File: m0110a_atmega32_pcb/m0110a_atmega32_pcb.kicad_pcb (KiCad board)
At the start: 2 copper layers, 17.8 x 53.3 mm, 9 parts, among them J1 Conn_01x40_Pin, J2 ISP, J3 Serial, U2 ATmega32A-M, Y1 8 MHz

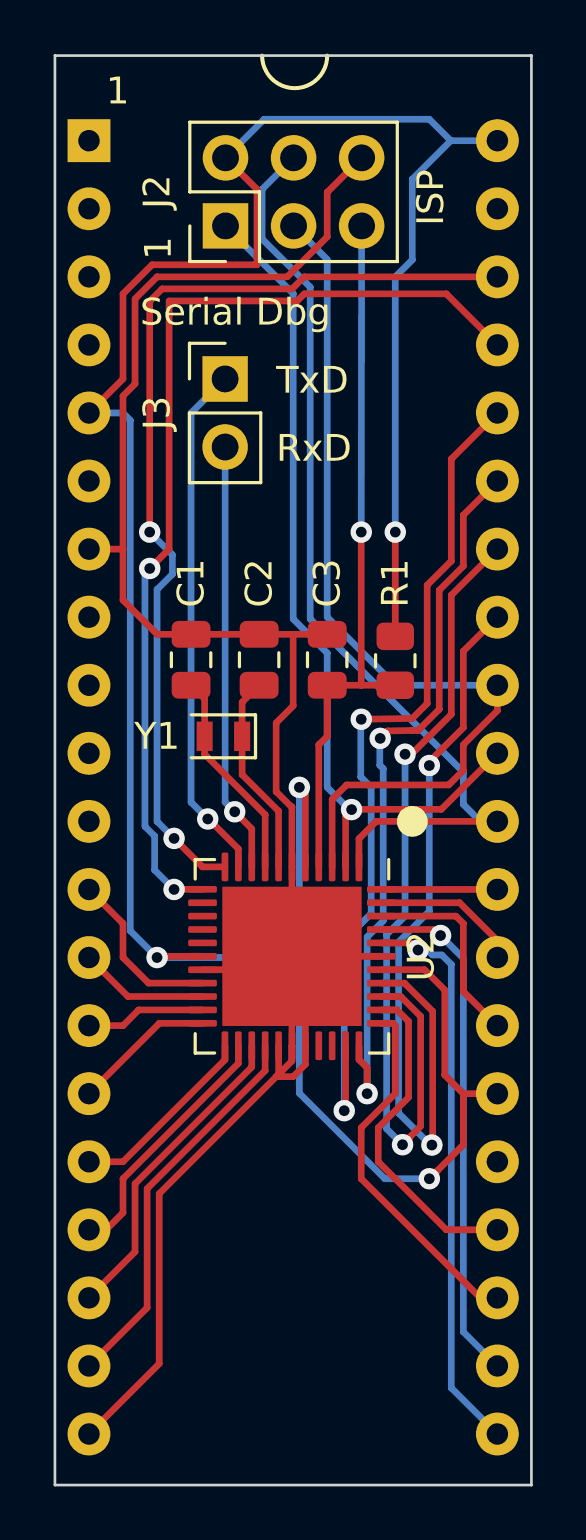
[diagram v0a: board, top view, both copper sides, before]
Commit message: Updated PCB to use more readily available parts
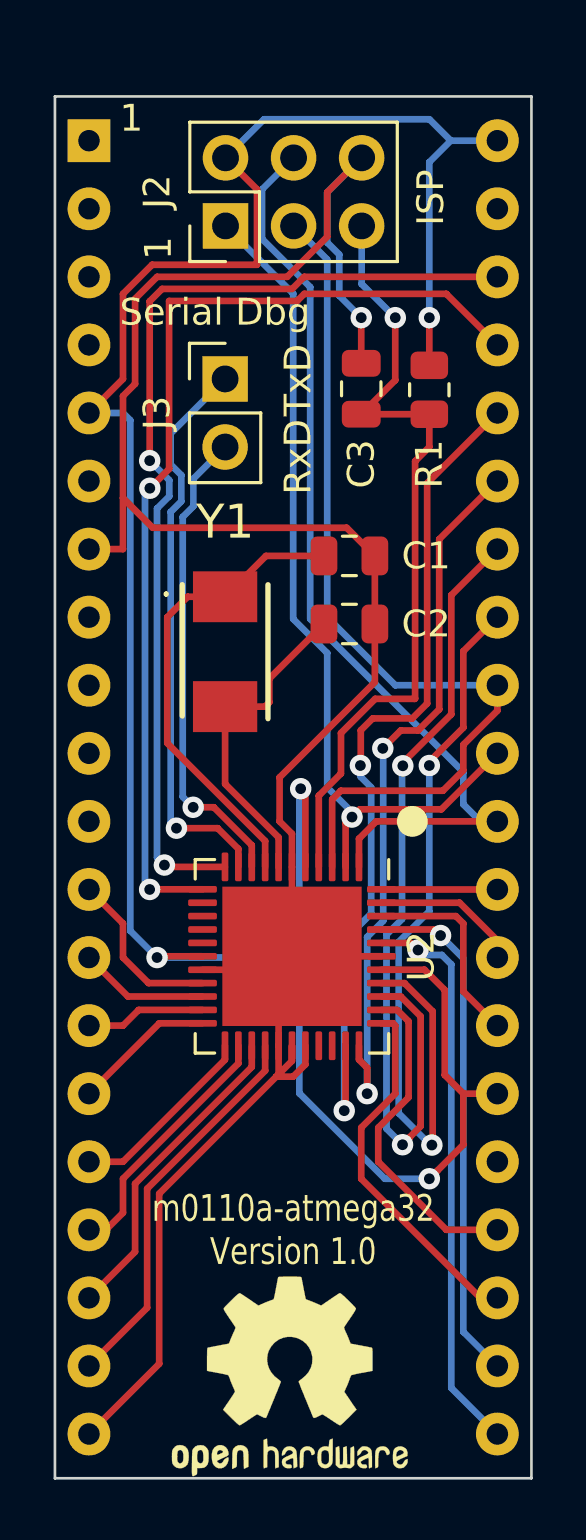
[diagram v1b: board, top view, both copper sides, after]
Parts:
- added REF**: OSHW-Logo2_9.8x8mm_SilkScreen, Symbol:OSHW-Logo2_9.8x8mm_SilkScreen, F.Cu at (151.0, 113.4)
- J1: footprint m0110a:Conn_2.54_W15.24mm -> m0110a:Header_2.54_W15.24mm
- Y1: value 8 MHz -> ABM3-8.000MHZ-D2Y-T; footprint Crystal:Crystal_SMD_2012-2Pin_2.0x1.2mm -> m0110a:ABM3
- moved C3 10.2 mm to (153.7, 76.6)
- moved R1 10.2 mm to (156.2, 76.6)
- moved C1 7.07 mm to (153.2, 82.8), turned to 180 degrees
- moved C2 3.62 mm to (153.2, 85.3), turned to 180 degrees
- moved Y1 3.16 mm to (148.6, 86.4), turned to -90 degrees
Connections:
- Y1 pad 1: Net-(U2-XTAL2) -> Net-(U2-XTAL1)
- Y1 pad 2: Net-(U2-XTAL1) -> Net-(U2-XTAL2)
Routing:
- net +5V: track 108.9 -> 98.1 mm
- net Net-(U2-XTAL1): track 7.92 -> 17.6 mm
- net GNDREF: track 81.4 -> 91.1 mm, vias 0 -> 1
- net Net-(U2-XTAL2): track 7.60 -> 12.3 mm
- net /RESET: track 26.6 -> 30.1 mm
- net /TXD: track 19.5 -> 21.3 mm
- net /RXD: track 16.1 -> 17.8 mm
- net /KB_DATA: track 36.6 -> 37.3 mm
- net /KB_CLK: track 37.0 -> 37.5 mm
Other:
- board size 17.8 x 53.3 mm -> 17.8 x 51.6 mm
- board text added: "github.com/esheffield/m0110a-atmega32"
- board text added: "m0110a-atmega32 Version 1.0"

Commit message: Switched from external to internal clocking
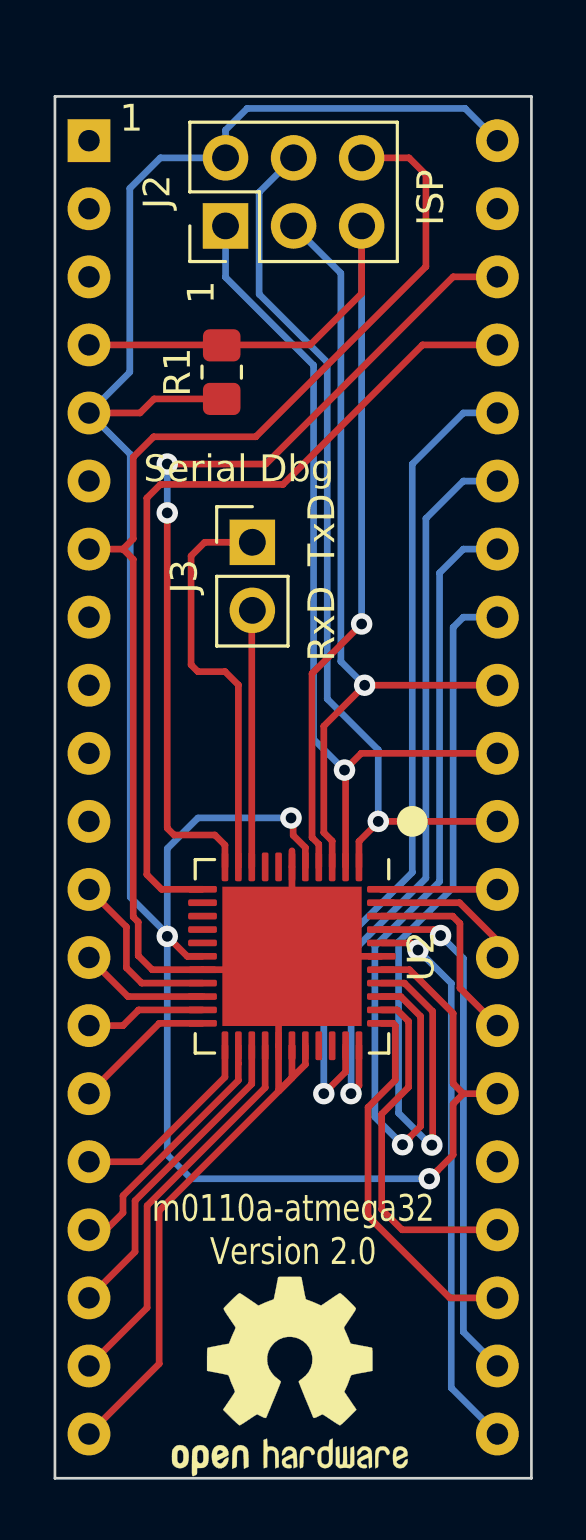
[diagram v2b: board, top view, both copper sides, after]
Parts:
- removed C1, C2: 22p, Capacitor_SMD:C_0805_2012Metric
- removed C3: 1u, Capacitor_SMD:C_0805_2012Metric
- removed Y1: ABM3-8.000MHZ-D2Y-T, m0110a:ABM3
- R1: footprint Resistor_SMD:R_0805_2012Metric -> Resistor_SMD:R_0805_2012Metric_Pad1.20x1.40mm_HandSolder
- moved R1 7.77 mm to (148.5, 75.9), turned to 90 degrees
- moved J3 6.18 mm to (149.6, 82.3)
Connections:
- J1 pad 4: unconnected-(J1-Pin_4-Pad4) -> RESET
- J2 pad 5: /RESET -> RESET
- R1 pad 2: /RESET -> RESET
- U2 pad 4: /RESET -> RESET
- U2 pad 7: Net-(U2-XTAL2) -> unconnected-(U2-XTAL2-Pad7)
- U2 pad 8: Net-(U2-XTAL1) -> unconnected-(U2-XTAL1-Pad8)
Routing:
- net RESET: track 0.00 -> 38.3 mm, vias 0 -> 1
- net /RESET: track 30.1 -> 0.00 mm, vias 1 -> 0
- net Net-(U2-XTAL1): track 17.6 -> 0.00 mm
- net Net-(U2-XTAL2): track 12.3 -> 0.00 mm
- net GNDREF: track 91.1 -> 81.2 mm, vias 1 -> 0
- net /RXD: track 17.8 -> 9.58 mm, vias 1 -> 0
- net /TXD: track 21.3 -> 15.4 mm, vias 1 -> 0
- net /KB_CLK: track 37.5 -> 31.8 mm, vias 2 -> 0
- net /KB_DATA: track 37.3 -> 32.0 mm
- net +5V: track 98.1 -> 93.2 mm, vias 4 -> 3
- net /ROW7: track 34.7 -> 31.8 mm, vias 0 -> 1
- net /ROW5: track 35.7 -> 33.6 mm, vias 0 -> 1
- net /CMD: track 32.3 -> 31.0 mm, vias 2 -> 1
- net /ROW9: track 31.0 -> 32.1 mm, vias 2 -> 1
- net /LOCK: track 12.4 -> 13.3 mm
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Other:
- board text added: "m0110a-atmega32 Version 2.0"
- board text removed: "m0110a-atmega32 Version 1.0"

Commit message: Removed unneeded resistor and ground connections
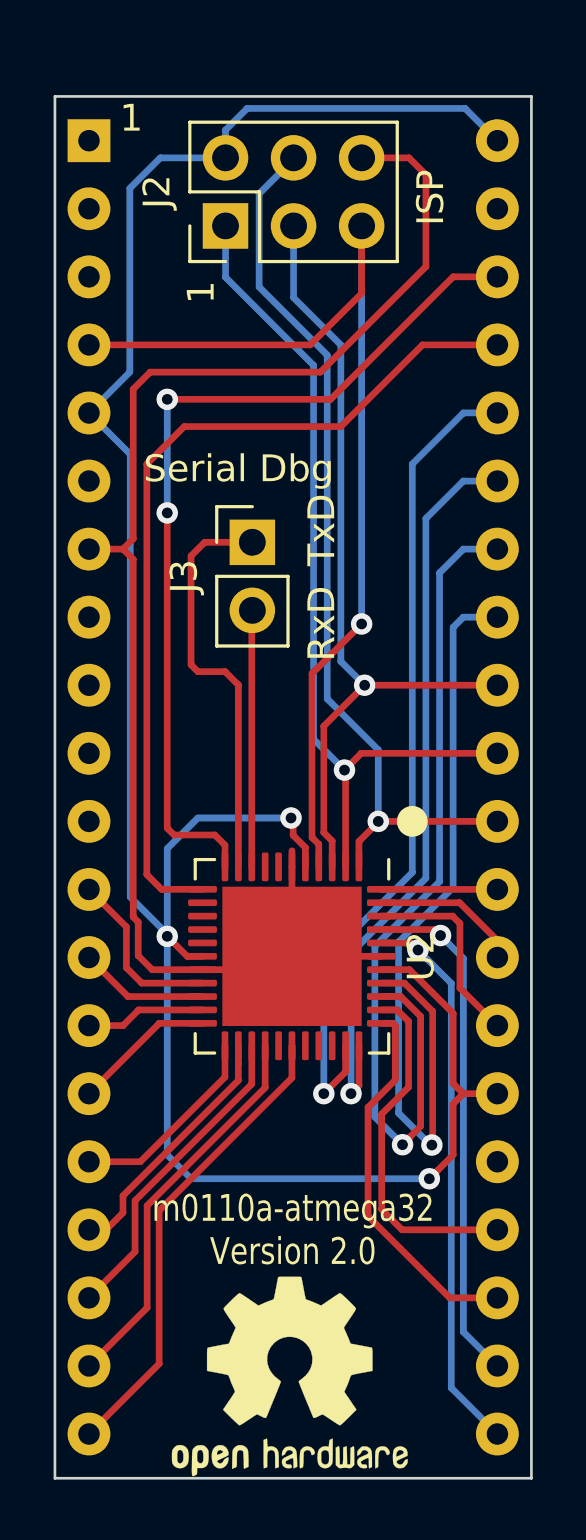
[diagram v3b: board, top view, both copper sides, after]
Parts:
- removed R1: 4k7, Resistor_SMD:R_0805_2012Metric_Pad1.20x1.40mm_HandSolder
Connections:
- U2 pad 27: GNDREF -> unconnected-(U2-AVCC-Pad27)
- U2 pad 29: GNDREF -> unconnected-(U2-AREF-Pad29)
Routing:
- net +5V: track 93.2 -> 88.1 mm
- net GNDREF: track 81.2 -> 76.1 mm
- net /KB_DATA: track 32.0 -> 33.4 mm
- net /KB_CLK: track 31.8 -> 32.5 mm

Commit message: Swapped data and clk for easier layout. V 2.1
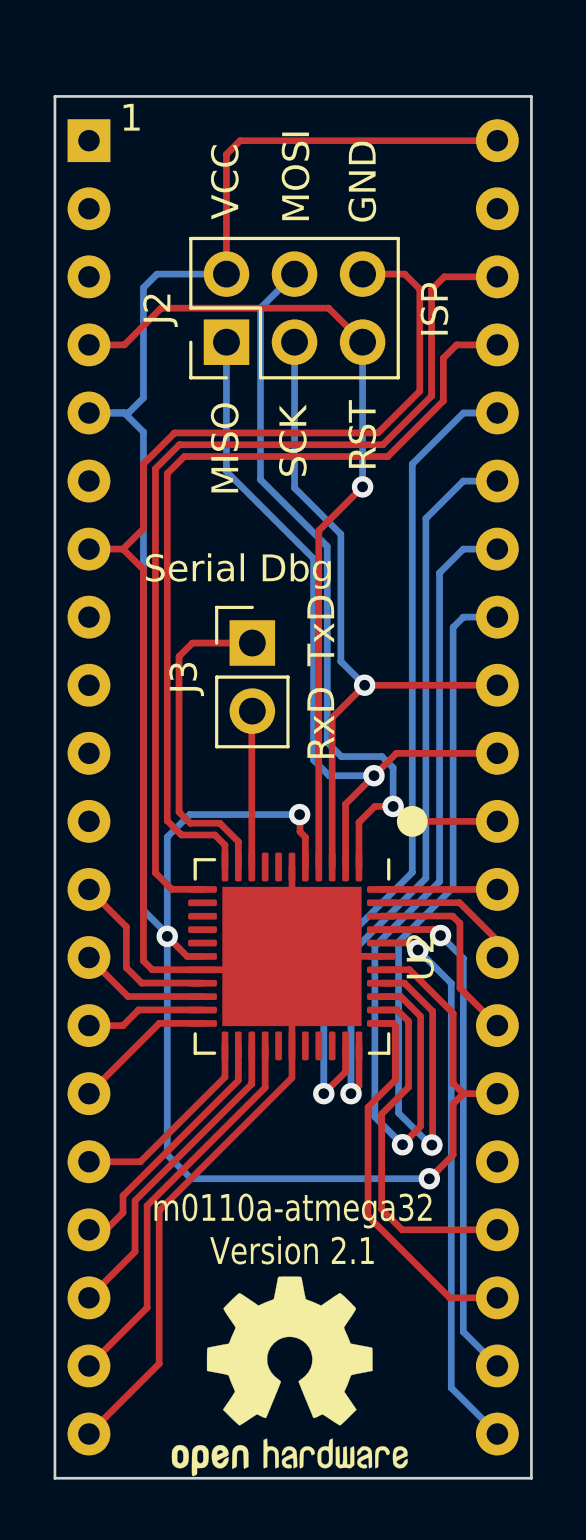
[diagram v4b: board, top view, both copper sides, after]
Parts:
- moved J2 4.34 mm to (148.6, 74.8)
- moved J3 3.76 mm to (149.6, 86.1)
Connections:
- U2 pad 11: /KB_DATA -> /KB_CLK
- U2 pad 12: /KB_CLK -> /KB_DATA
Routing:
- net RESET: track 38.3 -> 31.6 mm
- net /ROW7: track 31.8 -> 26.8 mm
- net GNDREF: track 76.1 -> 71.6 mm
- net /RXD: track 9.58 -> 5.82 mm
- net /ROW6: track 31.7 -> 28.2 mm
- net /TXD: track 15.4 -> 12.4 mm
- net /ROW5: track 33.6 -> 30.6 mm
- net /KB_DATA: track 33.4 -> 35.1 mm, vias 2 -> 0
- net /KB_CLK: track 32.5 -> 31.5 mm
- net +5V: track 88.1 -> 88.9 mm
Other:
- board text added: "GND"
- board text added: "MISO"
- board text added: "MOSI"
- board text added: "RST"
- board text added: "SCK"
- board text added: "VCC"
- board text added: "m0110a-atmega32 Version 2.1"
- board text removed: "m0110a-atmega32 Version 2.0"

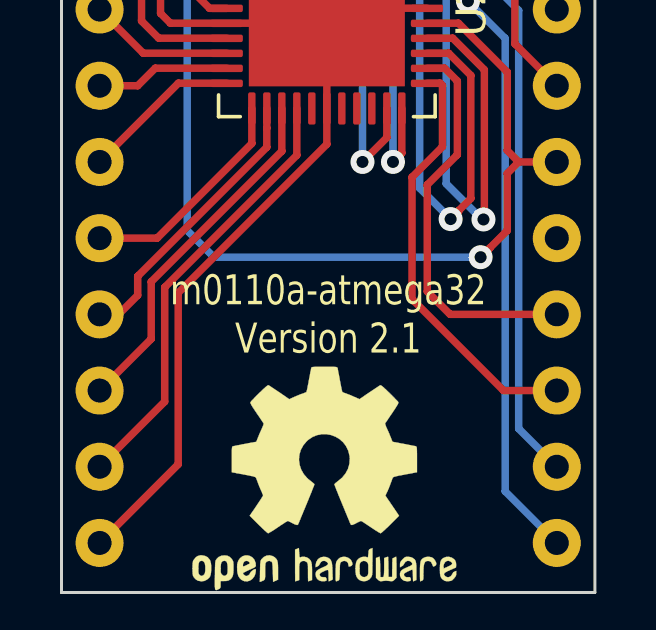
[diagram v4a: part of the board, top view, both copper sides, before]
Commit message: Added gerbers (PCBWay rules)
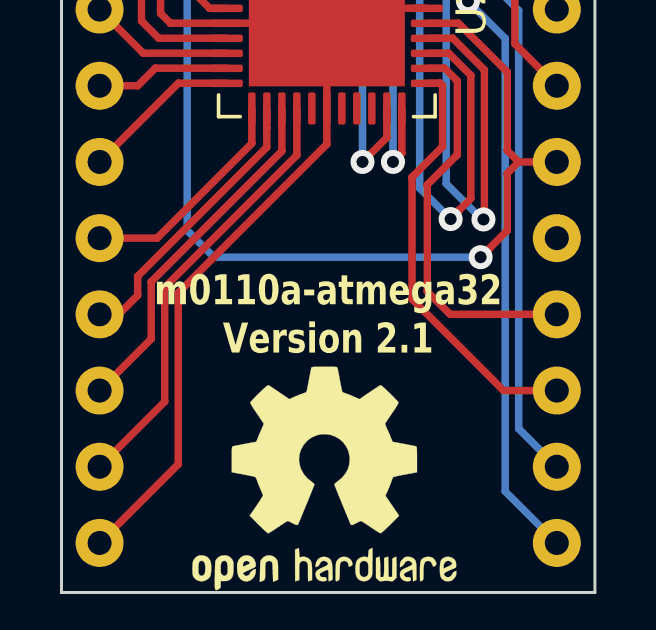
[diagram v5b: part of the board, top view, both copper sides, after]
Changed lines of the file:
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@@
     (0 "F.Cu" signal)
     (31 "B.Cu" signal)
-    (32 "B.Adhes" user "B.Adhesive")
-    (33 "F.Adhes" user "F.Adhesive")
     (34 "B.Paste" user)
     (35 "F.Paste" user)
@@
     (38 "B.Mask" user)
     (39 "F.Mask" user)
-    (40 "Dwgs.User" user "User.Drawings")
-    (41 "Cmts.User" user "User.Comments")
-    (42 "Eco1.User" user "User.Eco1")
-    (43 "Eco2.User" user "User.Eco2")
     (44 "Edge.Cuts" user)
     (45 "Margin" user)
@@
     (48 "B.Fab" user)
     (49 "F.Fab" user)
-    (50 "User.1" user)
-    (51 "User.2" user)
-    (52 "User.3" user)
-    (53 "User.4" user)
-    (54 "User.5" user)
-    (55 "User.6" user)
-    (56 "User.7" user)
-    (57 "User.8" user)
-    (58 "User.9" user)
   )
   (setup
@@
     )
     (pad_to_mask_clearance 0)
+    (solder_mask_min_width 0.1016)
     (pcbplotparams
       (layerselection 0x00010fc_ffffffff)
@@
       (usegerberattributes true)
       (usegerberadvancedattributes true)
-      (creategerberjobfile true)
+      (creategerberjobfile false)
       (dashed_line_dash_ratio 12.000000)
       (dashed_line_gap_ratio 3.000000)
@@
       (psa4output false)
       (plotreference true)
-      (plotvalue true)
+      (plotvalue false)
       (plotinvisibletext false)
       (sketchpadsonfab false)
-      (subtractmaskfromsilk false)
+      (subtractmaskfromsilk true)
       (outputformat 1)
       (mirror false)
-      (drillshape 1)
+      (drillshape 0)
       (scaleselection 1)
-      (outputdirectory "")
+      (outputdirectory "gerbers/")
     )
   )
@@
     (fp_line (start 3.5 3.5) (end -3.5 3.5)
       (stroke (width 0.1) (type solid)) (layer "F.Fab"))
-    (pad "" smd roundrect (at -1.95 -1.95 270) (size 1.05 1.05) (layers "F.Paste") (roundrect_rratio 0.238095))
-    (pad "" smd roundrect (at -1.95 -0.65 270) (size 1.05 1.05) (layers "F.Paste") (roundrect_rratio 0.238095))
-    (pad "" smd roundrect (at -1.95 0.65 270) (size 1.05 1.05) (layers "F.Paste") (roundrect_rratio 0.238095))
-    (pad "" smd roundrect (at -1.95 1.95 270) (size 1.05 1.05) (layers "F.Paste") (roundrect_rratio 0.238095))
-    (pad "" smd roundrect (at -0.65 -1.95 270) (size 1.05 1.05) (layers "F.Paste") (roundrect_rratio 0.238095))
-    (pad "" smd roundrect (at -0.65 -0.65 270) (size 1.05 1.05) (layers "F.Paste") (roundrect_rratio 0.238095))
-    (pad "" smd roundrect (at -0.65 0.65 270) (size 1.05 1.05) (layers "F.Paste") (roundrect_rratio 0.238095))
-    (pad "" smd roundrect (at -0.65 1.95 270) (size 1.05 1.05) (layers "F.Paste") (roundrect_rratio 0.238095))
-    (pad "" smd roundrect (at 0.65 -1.95 270) (size 1.05 1.05) (layers "F.Paste") (roundrect_rratio 0.238095))
-    (pad "" smd roundrect (at 0.65 -0.65 270) (size 1.05 1.05) (layers "F.Paste") (roundrect_rratio 0.238095))
-    (pad "" smd roundrect (at 0.65 0.65 270) (size 1.05 1.05) (layers "F.Paste") (roundrect_rratio 0.238095))
-    (pad "" smd roundrect (at 0.65 1.95 270) (size 1.05 1.05) (layers "F.Paste") (roundrect_rratio 0.238095))
-    (pad "" smd roundrect (at 1.95 -1.95 270) (size 1.05 1.05) (layers "F.Paste") (roundrect_rratio 0.238095))
-    (pad "" smd roundrect (at 1.95 -0.65 270) (size 1.05 1.05) (layers "F.Paste") (roundrect_rratio 0.238095))
-    (pad "" smd roundrect (at 1.95 0.65 270) (size 1.05 1.05) (layers "F.Paste") (roundrect_rratio 0.238095))
-    (pad "" smd roundrect (at 1.95 1.95 270) (size 1.05 1.05) (layers "F.Paste") (roundrect_rratio 0.238095))
+    (pad "" smd roundrect (at -1.95 -1.95 270) (size 1.05 1.05) (layers "F.Paste") (roundrect_rratio 0.2380952381))
+    (pad "" smd roundrect (at -1.95 -0.65 270) (size 1.05 1.05) (layers "F.Paste") (roundrect_rratio 0.2380952381))
+    (pad "" smd roundrect (at -1.95 0.65 270) (size 1.05 1.05) (layers "F.Paste") (roundrect_rratio 0.2380952381))
+    (pad "" smd roundrect (at -1.95 1.95 270) (size 1.05 1.05) (layers "F.Paste") (roundrect_rratio 0.2380952381))
+    (pad "" smd roundrect (at -0.65 -1.95 270) (size 1.05 1.05) (layers "F.Paste") (roundrect_rratio 0.2380952381))
+    (pad "" smd roundrect (at -0.65 -0.65 270) (size 1.05 1.05) (layers "F.Paste") (roundrect_rratio 0.2380952381))
+    (pad "" smd roundrect (at -0.65 0.65 270) (size 1.05 1.05) (layers "F.Paste") (roundrect_rratio 0.2380952381))
+    (pad "" smd roundrect (at -0.65 1.95 270) (size 1.05 1.05) (layers "F.Paste") (roundrect_rratio 0.2380952381))
+    (pad "" smd roundrect (at 0.65 -1.95 270) (size 1.05 1.05) (layers "F.Paste") (roundrect_rratio 0.2380952381))
+    (pad "" smd roundrect (at 0.65 -0.65 270) (size 1.05 1.05) (layers "F.Paste") (roundrect_rratio 0.2380952381))
+    (pad "" smd roundrect (at 0.65 0.65 270) (size 1.05 1.05) (layers "F.Paste") (roundrect_rratio 0.2380952381))
+    (pad "" smd roundrect (at 0.65 1.95 270) (size 1.05 1.05) (layers "F.Paste") (roundrect_rratio 0.2380952381))
+    (pad "" smd roundrect (at 1.95 -1.95 270) (size 1.05 1.05) (layers "F.Paste") (roundrect_rratio 0.2380952381))
+    (pad "" smd roundrect (at 1.95 -0.65 270) (size 1.05 1.05) (layers "F.Paste") (roundrect_rratio 0.2380952381))
+    (pad "" smd roundrect (at 1.95 0.65 270) (size 1.05 1.05) (layers "F.Paste") (roundrect_rratio 0.2380952381))
+    (pad "" smd roundrect (at 1.95 1.95 270) (size 1.05 1.05) (layers "F.Paste") (roundrect_rratio 0.2380952381))
     (pad "1" smd roundrect (at -3.3375 -2.5 270) (size 1.075 0.25) (layers "F.Cu" "F.Paste" "F.Mask") (roundrect_rratio 0.25)
       (net 33 "/ROW5") (pinfunction "PB5") (pintype "bidirectional"))
@@
   )
   (gr_text "m0110a-atmega32\nVersion 2.1" (at 151.13 109.347) (layer "F.SilkS")
-    (effects (font (size 1 0.8) (thickness 0.125)) (justify bottom))
+    (effects (font (size 1 0.8) (thickness 0.1524) bold) (justify bottom))
   )
   (gr_text "SCK" (at 151.7396 79.9084 90) (layer "F.SilkS")
